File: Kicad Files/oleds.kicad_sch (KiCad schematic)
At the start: 26 parts, among them J1 SPD_OLED, J14 R_OLED, J15 L_OLED, J2 HDG_OLED, J3 H_T_OLED, J4 ALT_OLED, J5 VSPEED_OLED

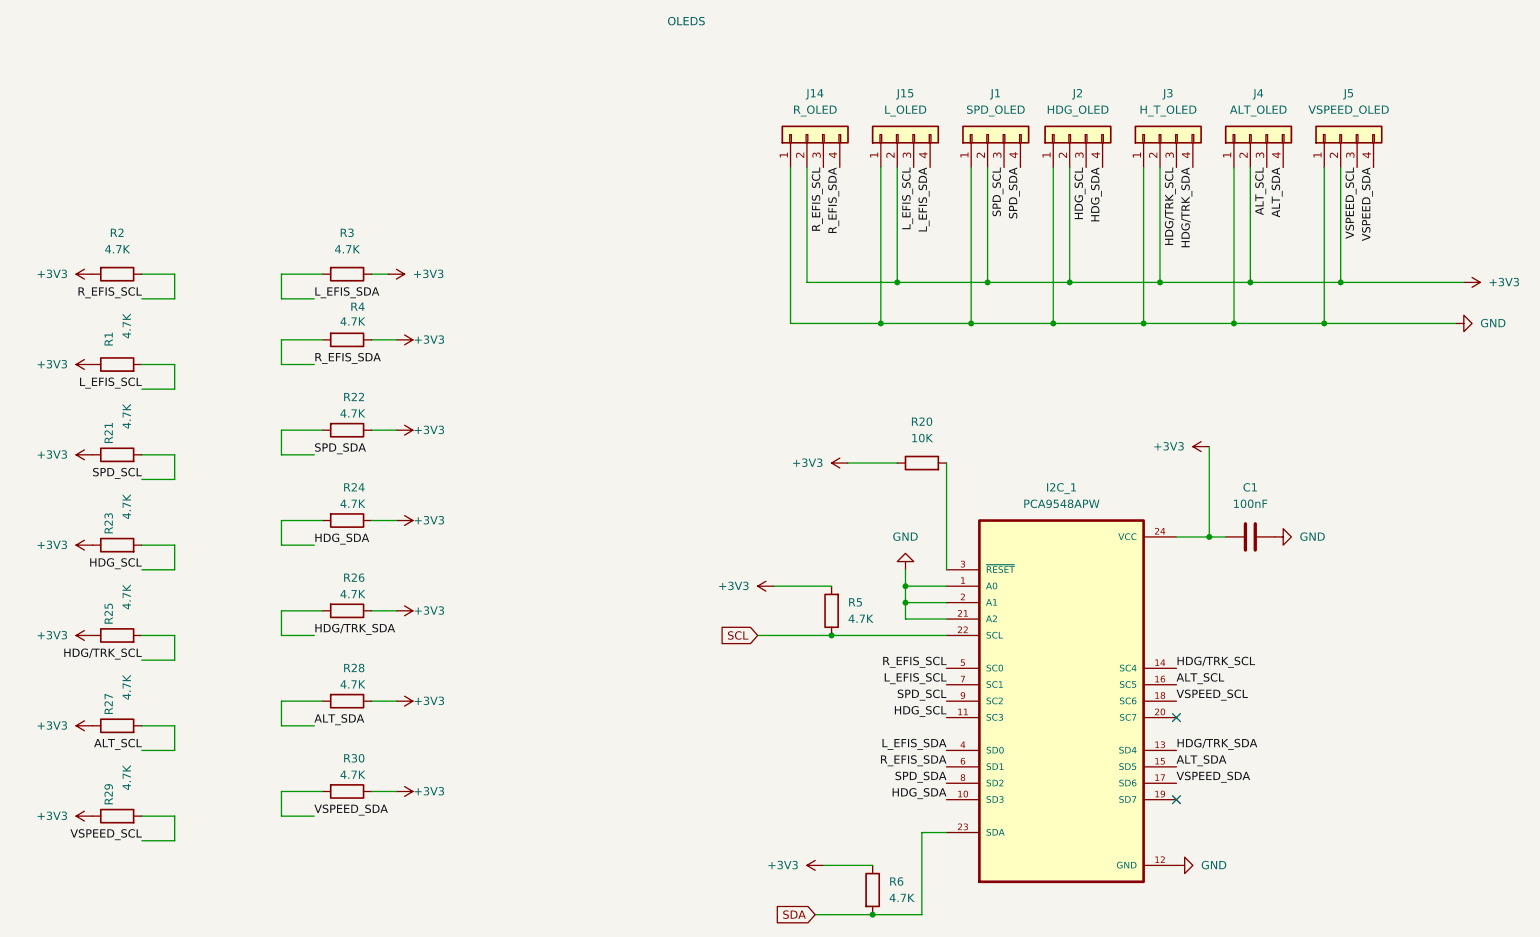
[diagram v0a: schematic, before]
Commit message: Fixed a serious error in the pcb design. I2C had a wrongly connected path between L an R EFIS OLEDs. Also added a dipswitch to select I2C address
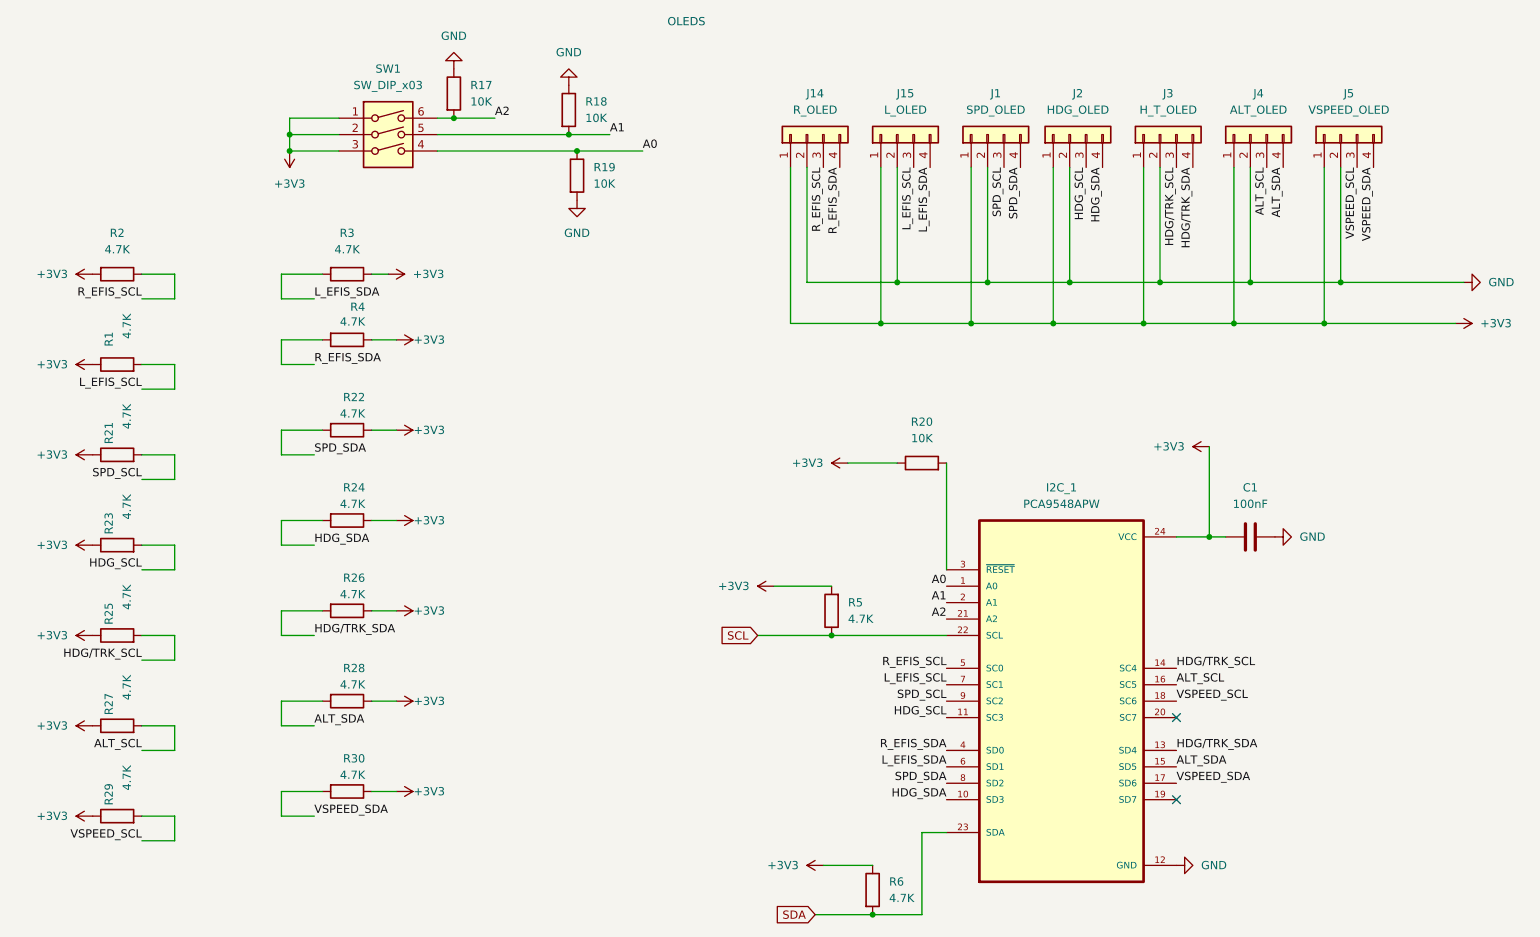
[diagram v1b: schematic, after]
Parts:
- added R17, R18, R19: 10K, Resistor_SMD:R_1206_3216Metric_Pad1.30x1.75mm_HandSolder, symbol Device:R
- added SW1: SW_DIP_x03, Button_Switch_THT:SW_DIP_SPSTx03_Slide_9.78x9.8mm_W7.62mm_P2.54mm, symbol Switch:SW_DIP_x03
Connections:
- net +3V3: now also J1.1 (Pin_1), J14.1 (Pin_1), J15.1 (Pin_1), J2.1 (Pin_1), J3.1 (Pin_1), J4.1 (Pin_1), J5.1 (Pin_1), SW1.1, SW1.2, SW1.3; no longer J1.2 (Pin_2), J14.2 (Pin_2), J15.2 (Pin_2), J2.2 (Pin_2), J3.2 (Pin_2), J4.2 (Pin_2), J5.2 (Pin_2)
- net GND: now also J1.2 (Pin_2), J14.2 (Pin_2), J15.2 (Pin_2), J2.2 (Pin_2), J3.2 (Pin_2), J4.2 (Pin_2), J5.2 (Pin_2), R17.1, R18.1, R19.2; no longer I2C_1.1 (A0), I2C_1.2 (A1), I2C_1.21 (A2), J1.1 (Pin_1), J14.1 (Pin_1), J15.1 (Pin_1), J2.1 (Pin_1), J3.1 (Pin_1), J4.1 (Pin_1), J5.1 (Pin_1)
- net L_EFIS_SDA: now also I2C_1.6 (SD1); no longer I2C_1.4 (SD0)
- net R_EFIS_SDA: now also I2C_1.4 (SD0); no longer I2C_1.6 (SD1)
- new net A0: I2C_1.1 (A0), R19.1, SW1.4
- new net A1: I2C_1.2 (A1), R18.2, SW1.5
- new net A2: I2C_1.21 (A2), R17.2, SW1.6

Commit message: Complete rework of panels to be printed facedown. Important: change the order of the colors as Grey, White, Black, Transparent if using a Bambulab P1S/X1C ALso corrected some issue with the PCB (optional, you can print the FCU without using my pcb)
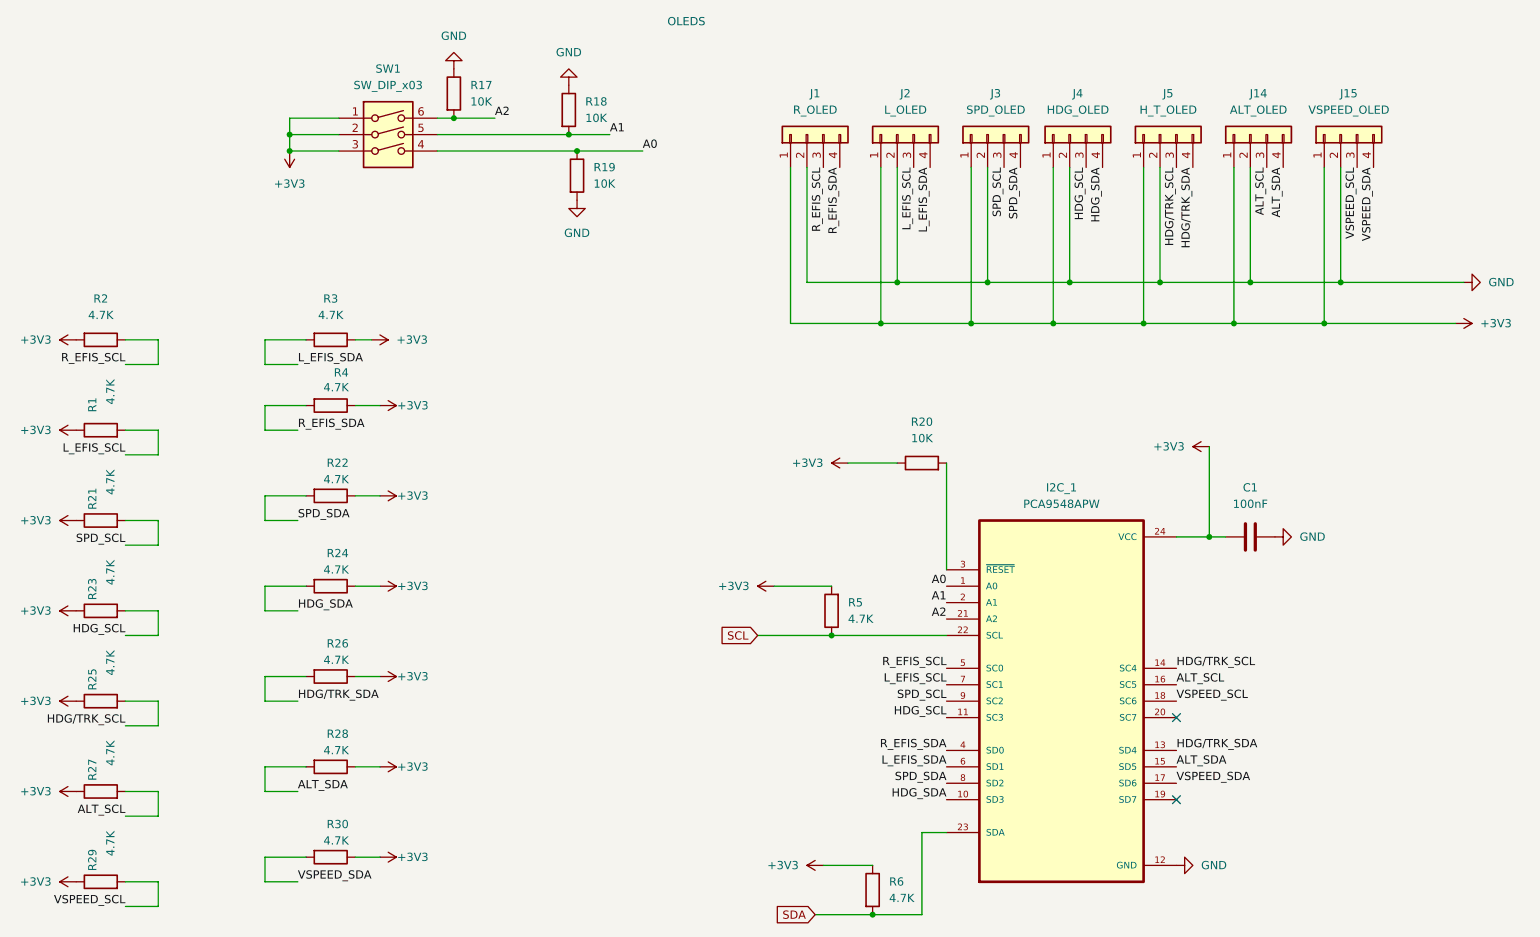
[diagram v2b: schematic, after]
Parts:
- I2C_1: footprint SFLibrary:SOP65P640X120-24N -> PCM_SFLibrary:SOP65P640X120-24N
- renumbered J14 to J1, J4 to J14, J5 to J15, J15 to J2, J1 to J3, J2 to J4, J3 to J5
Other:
- moved on the sheet: R1, R2, R21, R22, R23, R24, R25, R26, R27, R28, R29, R3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
